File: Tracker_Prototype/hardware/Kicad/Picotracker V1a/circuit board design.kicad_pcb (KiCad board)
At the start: 2 copper layers, 33.3 x 20.1 mm, 29 parts, among them J1 Conn_01x06, J2 GND, J3 3.3V, SW1 SW_Push, U1 MAX-M8C, U3 CMWX1ZZABZ-078, U6 MS5607-02BA

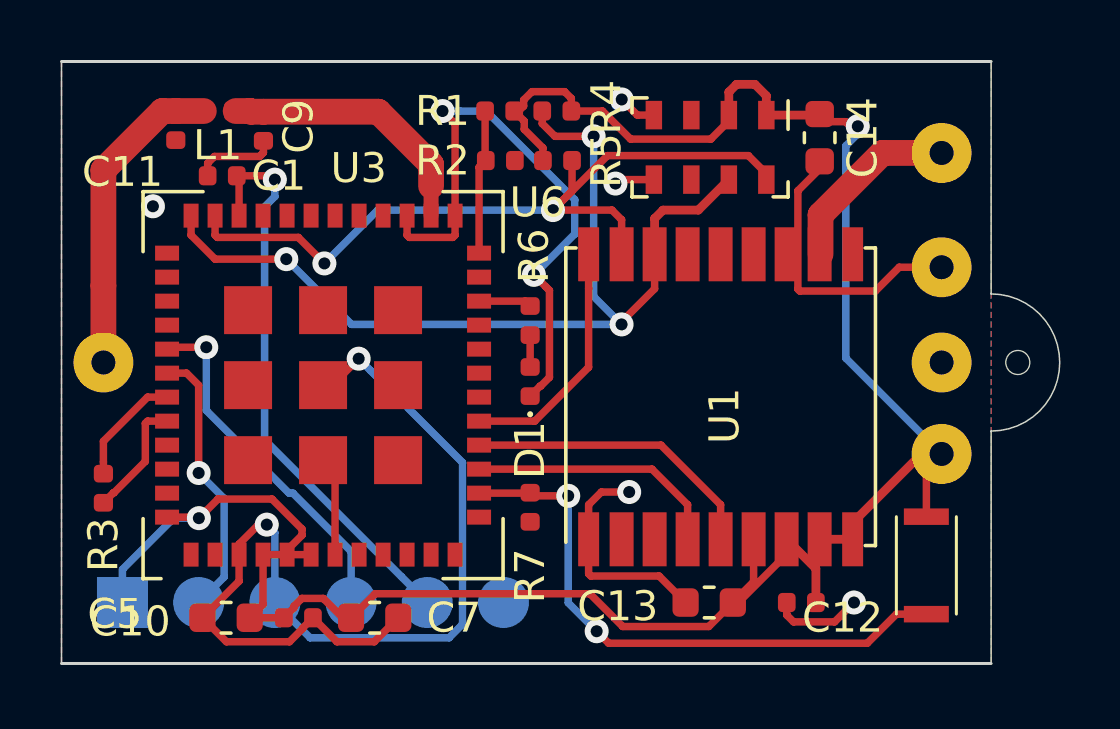
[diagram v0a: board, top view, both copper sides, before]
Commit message: Finished the design for the batteryless version
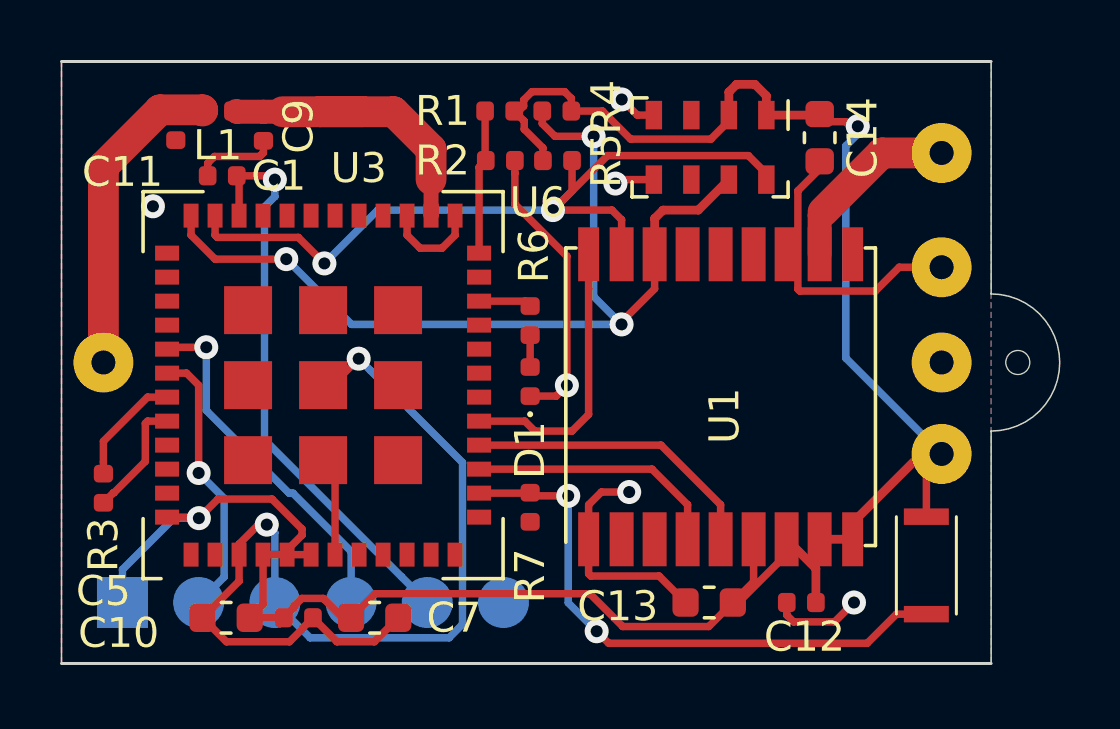
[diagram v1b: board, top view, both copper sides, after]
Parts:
- added G***: LOGO, flight-computer:ICSS_Logo, B.Cu at (280.5, 166.9)
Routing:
- net GND: track 86.3 -> 79.3 mm, vias 9 -> 8
- net Net-(C9-Pad1): track 8.96 -> 11.0 mm
- net /GPS_SAFEBOOT: track 8.16 -> 9.36 mm
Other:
- board text added: "PicoTracker LoRa Imperial College Space Society Medad Newman, Richard Ibbotson"

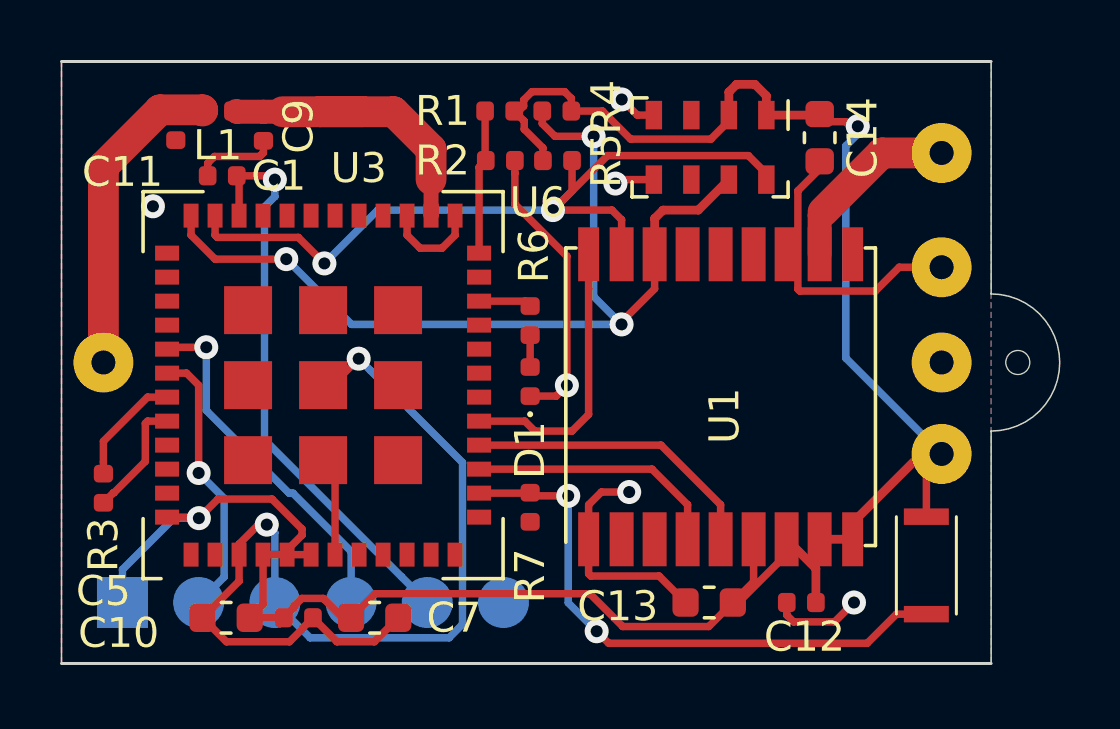
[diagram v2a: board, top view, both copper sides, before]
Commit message: updated circuit of b variant for low power voltage measurment. Made a variant tcxo enable controllable
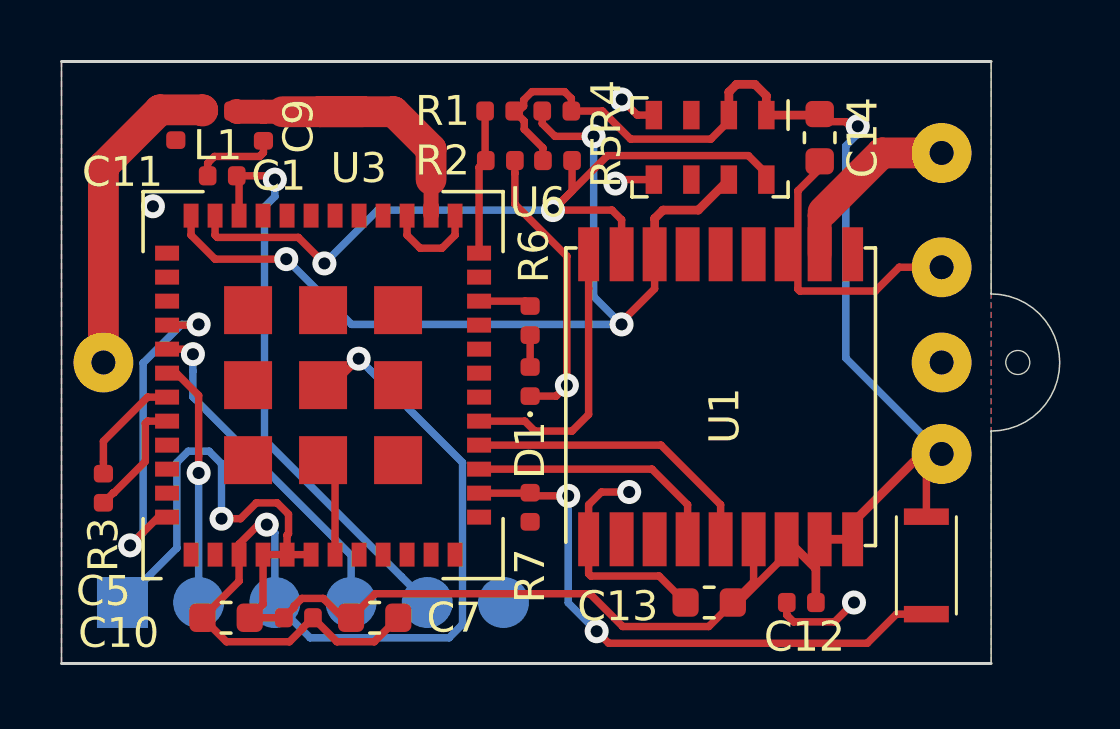
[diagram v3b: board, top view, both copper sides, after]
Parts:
- removed G***: LOGO, flight-computer:ICSS_Logo
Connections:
- U3 pad 40: (no net) -> /TCXO_EN
- U3 pad 48: +3V3 -> /TCXO_EN
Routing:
- net /TCXO_EN: track 0.00 -> 11.3 mm, vias 0 -> 2
- net +3V3: track 79.5 -> 81.9 mm
- net /SWCLK: track 9.17 -> 8.26 mm
- net /SWDIO: track 11.9 -> 11.4 mm

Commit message: Routed most of the b variant of the board
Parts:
- added J4: ICSS Logo, flight-computer:ICSS_Logo, B.Cu at (280.0, 167.4)

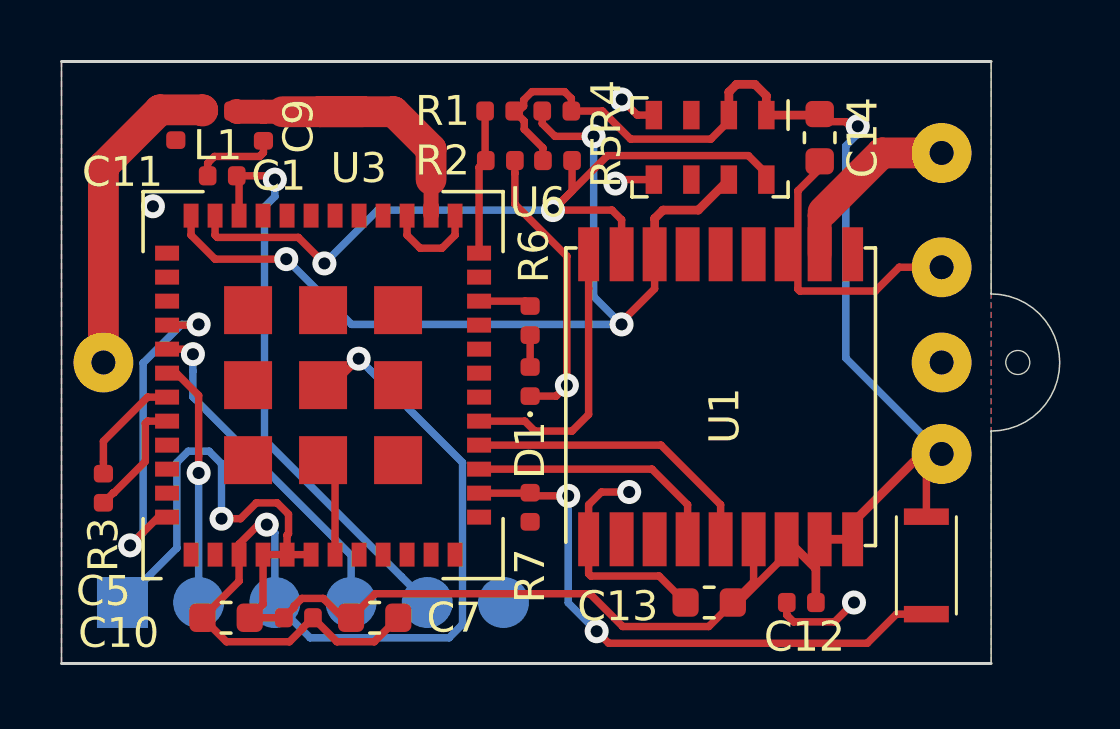
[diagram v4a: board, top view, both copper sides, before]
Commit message: rerouted the "a" variant to place the RF output pin of abz module closer to antenna
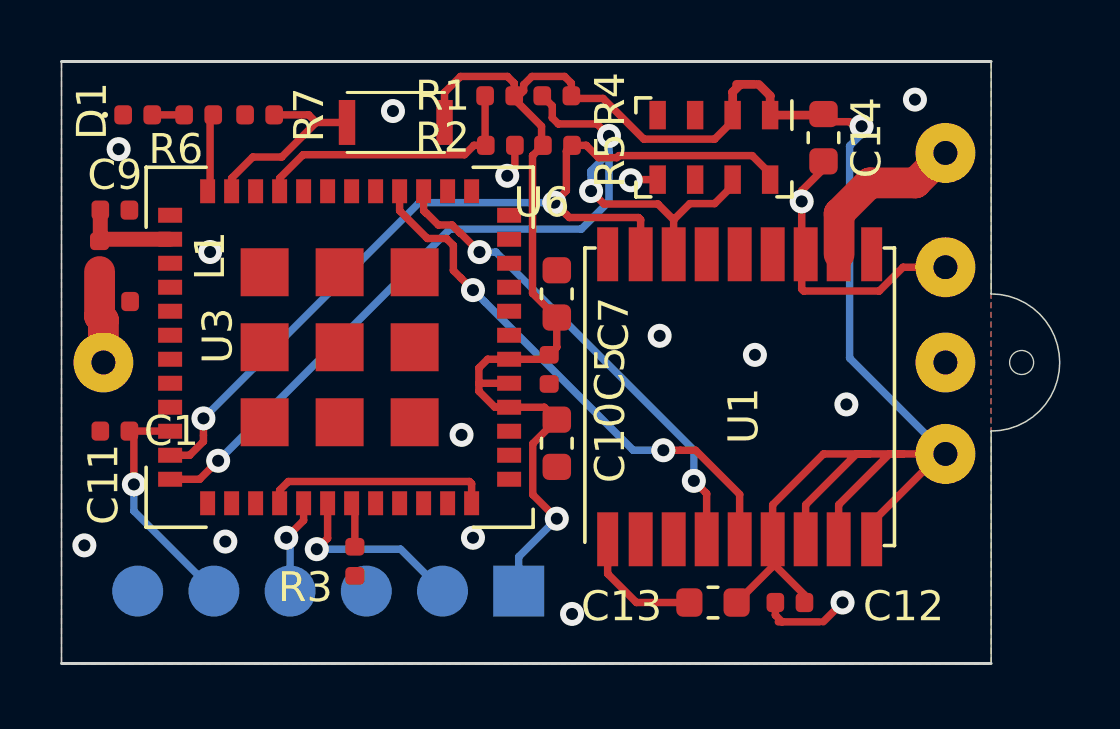
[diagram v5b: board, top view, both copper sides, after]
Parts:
- moved SW1 23.7 mm to (277.4, 162.1), turned to 180 degrees
- moved R7 15.9 mm to (273.3, 161.8), turned to 180 degrees
- moved D1 15.8 mm to (269.2, 161.8), turned to 0 degrees
- moved J1 13.2 mm to (281.9, 177.7), turned to 90 degrees
- moved R6 13.0 mm to (271.3, 161.8), turned to 0 degrees
- moved C10 12.5 mm to (283.2, 172.7), turned to 270 degrees
- moved C7 12.4 mm to (283.2, 167.8), turned to 90 degrees
- moved C5 11.8 mm to (283.0, 170.3), turned to 270 degrees
- moved C1 9.23 mm to (268.5, 172.3)
- moved R3 8.73 mm to (276.5, 176.7)
- moved L1 6.24 mm to (268.0, 166.5), turned to 90 degrees
- moved C11 6.20 mm to (268.5, 168.0), turned to 0 degrees
- moved C9 5.69 mm to (268.5, 165.0), turned to 0 degrees
- moved U3 1.38 mm to (276.0, 169.5), turned to 180 degrees
- moved U1 0.63 mm to (289.3, 171.2)
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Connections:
- U1 pad 18: /GPS_SAFEBOOT -> (no net)
- U3 pad 14: /SWITCH -> (no net)
- U3 pad 17: /GPS_SAFEBOOT -> (no net)
- U3 pad 21: (no net) -> /V_SOLAR
- U3 pad 22: /LED -> (no net)
- U3 pad 23: (no net) -> /SWITCH
- U3 pad 24: /V_SOLAR -> /LED
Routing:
- net GND: track 79.3 -> 18.8 mm, vias 8 -> 16
- net /SWITCH: track 19.5 -> 6.56 mm, vias 2 -> 0
- net /RESET: track 19.2 -> 7.86 mm
- net /GPS_SAFEBOOT: track 9.36 -> 0.00 mm
- net /SWDIO: track 11.4 -> 3.22 mm
- net /GPS_EXTINT: track 10.0 -> 17.9 mm, vias 0 -> 2
- net Net-(AE1-Pad1): track 10.7 -> 3.08 mm
- net Net-(C9-Pad1): track 11.0 -> 3.43 mm
- net /GPS_TIMEPULSE: track 8.59 -> 16.1 mm, vias 0 -> 2
- net /V_SOLAR: track 4.84 -> 9.42 mm
- net /TCXO_EN: track 11.3 -> 7.64 mm, vias 2 -> 0
- net /I2C1_SCL: track 26.8 -> 30.4 mm
- net Net-(R3-Pad1): track 3.81 -> 1.49 mm
- net /SWCLK: track 8.26 -> 6.45 mm
- net +3V3: track 81.9 -> 80.9 mm
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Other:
- board text removed: "PicoTracker LoRa Imperial College Space Society Medad Newman, Richard Ibbotson"

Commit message: Finished the layout of both the a and b variants. Silkscreen also done
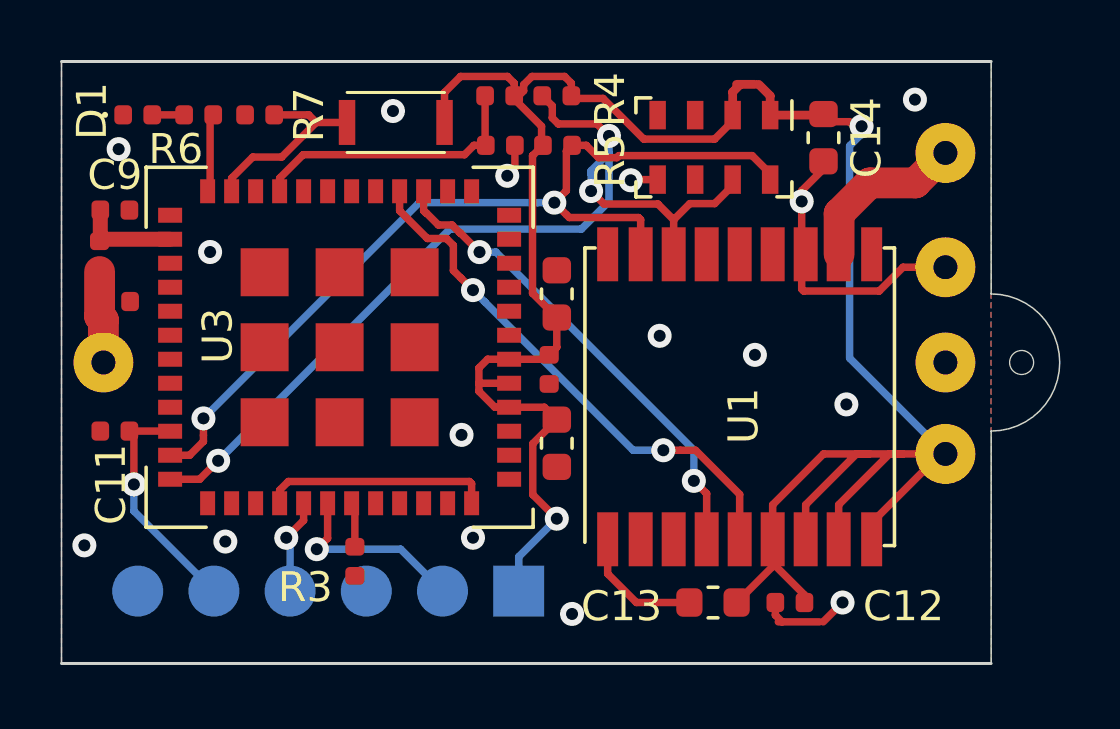
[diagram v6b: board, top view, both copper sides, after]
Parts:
- moved J4 0.99 mm to (280.8, 166.8)
- renumbered J3 to +SOL, J2 to GND
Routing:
- net GND: vias 16 -> 15
- net (no net): vias 0 -> 1
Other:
- board text added: "PicoTracker LoRa V1a Imperial College Space Society Medad Newman, Richard Ibbotson"
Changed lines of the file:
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@@
   (general
     (thickness 0.6)
-    (drawings 11)
+    (drawings 12)
     (tracks 246)
     (zones 0)
@@
   )
   (layers
-    (0 F.Cu signal)
+    (0 F.Cu signal hide)
     (31 B.Cu signal)
     (32 B.Adhes user hide)
@@
     (35 F.Paste user hide)
     (36 B.SilkS user)
-    (37 F.SilkS user)
+    (37 F.SilkS user hide)
     (38 B.Mask user hide)
     (39 F.Mask user hide)
@@
     (tags connector)
     (attr virtual)
-    (fp_text reference J3 (at 0 2.413 180) (layer B.SilkS)
+    (fp_text reference +SOL (at 3.048 0.508 180) (layer B.SilkS)
       (effects (font (size 1 1) (thickness 0.15)) (justify mirror))
     )
@@
     (tags connector)
     (attr virtual)
-    (fp_text reference J2 (at 0 2.667 180) (layer B.SilkS)
+    (fp_text reference GND (at 0.127 2.794 180) (layer B.SilkS)
       (effects (font (size 1 1) (thickness 0.15)) (justify mirror))
     )
@@
     (tags "lga land grid array")
     (attr smd)
-    (fp_text reference U6 (at 1.837 5.745 180) (layer F.SilkS)
-      (effects (font (size 1 1) (thickness 0.15)))
+    (fp_text reference U6 (at 3.615 -0.224 180) (layer F.SilkS) hide
+      (effects (font (size 1 1) (thickness 0.15)) (justify mirror))
     )
     (fp_text value MS5607-02BA (at 0 3.65 90) (layer F.Fab)
@@
     (tags capacitor)
     (attr smd)
-    (fp_text reference C10 (at -0.0255 -1.778 90) (layer F.SilkS)
+    (fp_text reference C10 (at 0.2285 -1.778 90) (layer F.SilkS) hide
       (effects (font (size 1 1) (thickness 0.15)))
     )
@@
     (tags capacitor)
     (attr smd)
-    (fp_text reference C7 (at -1.016 1.905 90) (layer F.SilkS)
+    (fp_text reference C7 (at -0.635 1.778 270) (layer F.SilkS) hide
       (effects (font (size 1 1) (thickness 0.15)))
     )
@@
     (tags capacitor)
     (attr smd)
-    (fp_text reference C5 (at 0.15 -2.032 90) (layer F.SilkS)
+    (fp_text reference C5 (at 0.15 -2.032 90) (layer F.SilkS) hide
       (effects (font (size 1 1) (thickness 0.15)))
     )
@@
     (tags capacitor)
     (attr smd)
-    (fp_text reference C1 (at -1.882 0) (layer F.SilkS)
+    (fp_text reference C1 (at -1.882 0) (layer F.SilkS) hide
       (effects (font (size 1 1) (thickness 0.15)))
     )
@@
   )
   (module flight-computer:ICSS_Logo (layer B.Cu)
-    (at 280.035 167.386 180)
+    (at 280.797 166.751 180)
     (fp_text reference J4 (at 0 0) (layer B.SilkS) hide
       (effects (font (size 1.524 1.524) (thickness 0.3)) (justify mirror))
@@
     (tags Switch)
     (attr smd)
-    (fp_text reference SW1 (at -0.127 0 180) (layer B.SilkS)
+    (fp_text reference SW1 (at -0.127 0 180) (layer B.SilkS) hide
       (effects (font (size 1.27 1.27) (thickness 0.254)) (justify mirror))
     )
@@
     (tags resistor)
     (attr smd)
-    (fp_text reference R2 (at -1.928 -0.254 180) (layer F.SilkS)
+    (fp_text reference R2 (at -1.928 -0.254 180) (layer F.SilkS) hide
       (effects (font (size 1 1) (thickness 0.15)))
     )
@@
     (tags resistor)
     (attr smd)
-    (fp_text reference R1 (at 1.905 0) (layer F.SilkS)
+    (fp_text reference R1 (at 1.905 0) (layer F.SilkS) hide
       (effects (font (size 1 1) (thickness 0.15)))
     )
@@
     (tags capacitor)
     (attr smd)
-    (fp_text reference C11 (at -0.404 6.096 270) (layer F.SilkS)
+    (fp_text reference C11 (at -0.15 6.096 270) (layer F.SilkS)
       (effects (font (size 1 1) (thickness 0.15)))
     )
@@
     (tags capacitor)
     (attr smd)
-    (fp_text reference L1 (at 0 3.683 90) (layer F.SilkS)
+    (fp_text reference L1 (at 0 3.683 90) (layer F.SilkS) hide
       (effects (font (size 1 1) (thickness 0.15)))
     )
@@
       (rotate (xyz 0 0 0))
     )
+  )
+  (gr_text "PicoTracker LoRa V1a\nImperial College Space Society\nMedad Newman, Richard Ibbotson " (at 281.051 172.72) (layer B.SilkS)
+    (effects (font (size 1 1) (thickness 0.15)) (justify mirror))
   )
   (dimension 10.033 (width 0.15) (layer Dwgs.User)
@@
   (segment (start 291.372999 164.684001) (end 291.372999 167.606001) (width 0.25) (layer F.Cu) (net 1))
   (via (at 291.372999 164.684001) (size 0.8) (drill 0.4) (layers F.Cu B.Cu) (net 1))
-  (via (at 280.035 172.466) (size 0.8) (drill 0.4) (layers F.Cu B.Cu) (net 1))
+  (via (at 280.035 172.466) (size 0.8) (drill 0.4) (layers F.Cu B.Cu) (net 0))
   (via (at 271.653 166.37) (size 0.8) (drill 0.4) (layers F.Cu B.Cu) (net 1))
   (via (at 267.462 176.149) (size 0.8) (drill 0.4) (layers F.Cu B.Cu) (net 1))

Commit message: sent off designs
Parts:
- moved J4 0.13 mm to (280.9, 166.8)
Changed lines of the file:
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@@
       (drillshape 0)
       (scaleselection 1)
-      (outputdirectory "D:/Long term storage and temp/dead weight program downloads/Flight computer V1.1 gerbers/"))
+      (outputdirectory "D:/Long term storage and temp/dead weight program downloads/lora tracker outputs/loratracker v1a/"))
   )
   (net 0 "")
@@
   )
   (module flight-computer:ICSS_Logo (layer B.Cu)
-    (at 280.797 166.751 180)
+    (at 280.924 166.751 180)
     (fp_text reference J4 (at 0 0) (layer B.SilkS) hide
       (effects (font (size 1.524 1.524) (thickness 0.3)) (justify mirror))
